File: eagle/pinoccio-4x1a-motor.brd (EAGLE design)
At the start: 25.4 x 43.2 mm, 27 parts, among them IC1 74LVC1G04DBV, IC2 74LVC1G04DBV, IC3 74LVC1G04DBV, IC4 74LVC1G04DBV, J1 POWER_JACKPTH, U1 TB6621FNG, U2 TB6621FNG

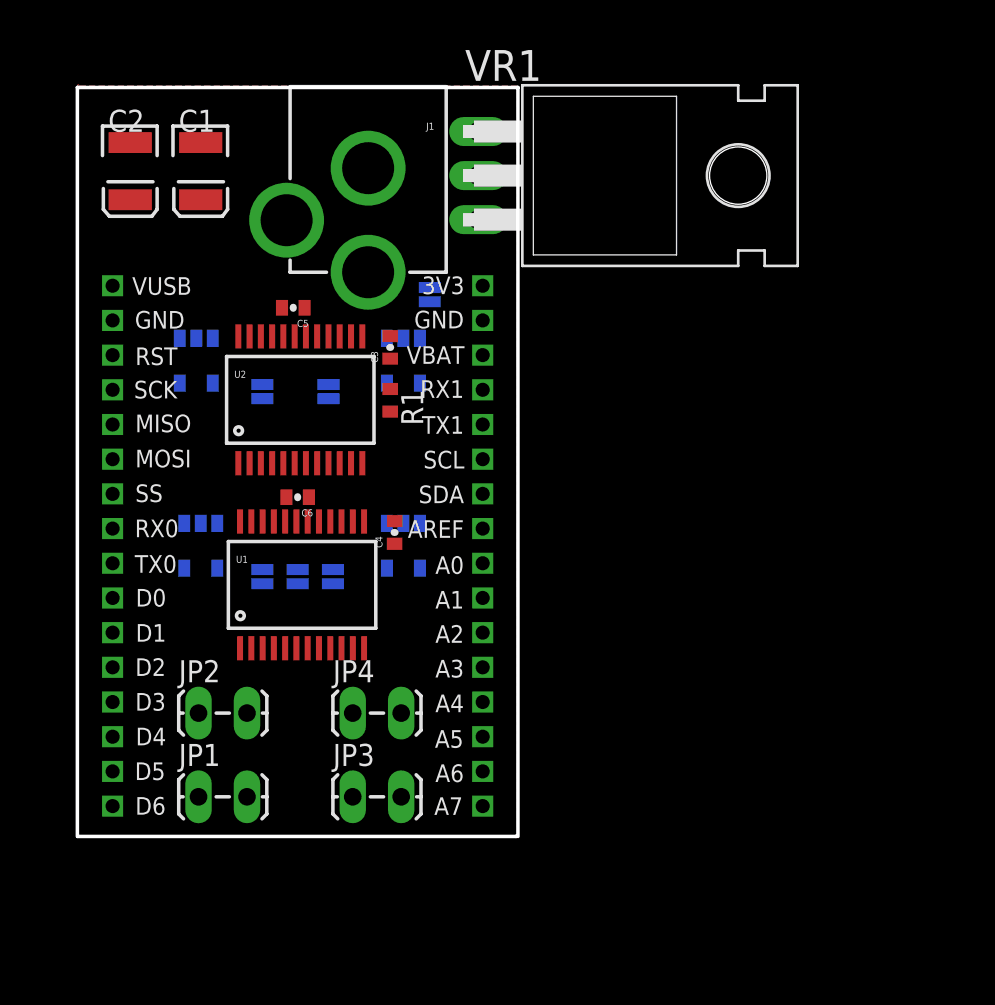
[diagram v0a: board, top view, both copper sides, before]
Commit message: Change layout onto an Arduino shield compatible board.
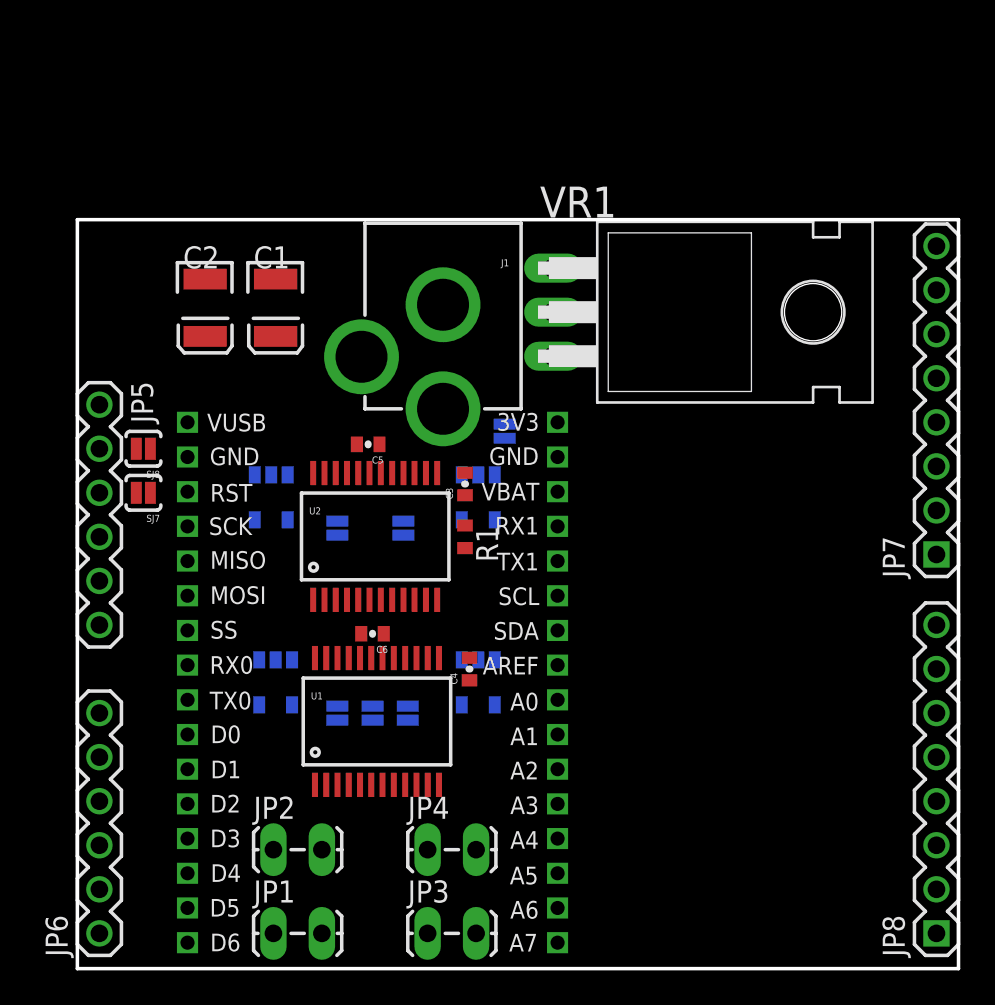
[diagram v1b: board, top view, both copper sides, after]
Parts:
- added JP5: Power, SparkFun:1X06
- added JP6: Analog, SparkFun:1X06
- added JP7: Digital2, SparkFun:1X08
- added JP8: Digital1, SparkFun:1X08
- added SJ7, SJ8: SOLDERJUMPERNC2, SparkFun-Passives:SJ_2S-NOTRACE
- moved C4 8.98 mm to (22.6, 17.3)
- moved C5 8.98 mm to (16.8, 30.2)
- moved C6 8.98 mm to (17.0, 19.3)
- moved J1 8.98 mm to (21.1, 46.0)
- moved JP3 8.98 mm to (20.3, 2.03)
- moved JP4 8.98 mm to (20.3, 6.86)
- moved SJ1 8.98 mm to (15.0, 14.7)
- moved SJ2 8.98 mm to (19.1, 14.7)
- moved SJ3 8.98 mm to (15.0, 25.4)
- moved SJ4 8.98 mm to (18.8, 25.4)
- moved SJ5 8.98 mm to (17.0, 14.7)
- moved SJ6 8.98 mm to (24.6, 31.0)
- moved U2 8.98 mm to (17.2, 24.9)
- moved C3 8.98 mm to (22.4, 27.9)
- moved IC2 8.98 mm to (23.1, 16.5)
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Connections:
- new net 3.3V: JP5.2, SJ8.2
- new net 5V: JP5.3, SJ7.2
- new net D10: JP7.3
- new net D11: JP7.4
- new net D12: JP7.5
- new net D13: JP7.6
- new net D7: JP8.8
- new net D8: JP7.1
- new net D9: JP7.2
- net A0: now also JP6.6
- net A1: now also JP6.5
- net A2: now also JP6.4
- net A3: now also JP6.3
- net A4: now also JP6.2
- net A5: now also JP6.1
- net AREF: now also JP7.8
- net D0: now also JP8.1
- net D1: now also JP8.2
- net D2: now also JP8.3
- net D3: now also JP8.4
- net D4: now also JP8.5
- net D5: now also JP8.6
- net D6: now also JP8.7
- net GND: now also JP5.4, JP5.5, JP7.7
- net RESET: now also JP5.1
- net VCC-AE: now also SJ7.1, SJ8.1
- net VUSB: now also JP5.6
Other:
- board size 25.4 x 43.2 mm -> 50.8 x 43.2 mm

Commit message: High current traces routed.
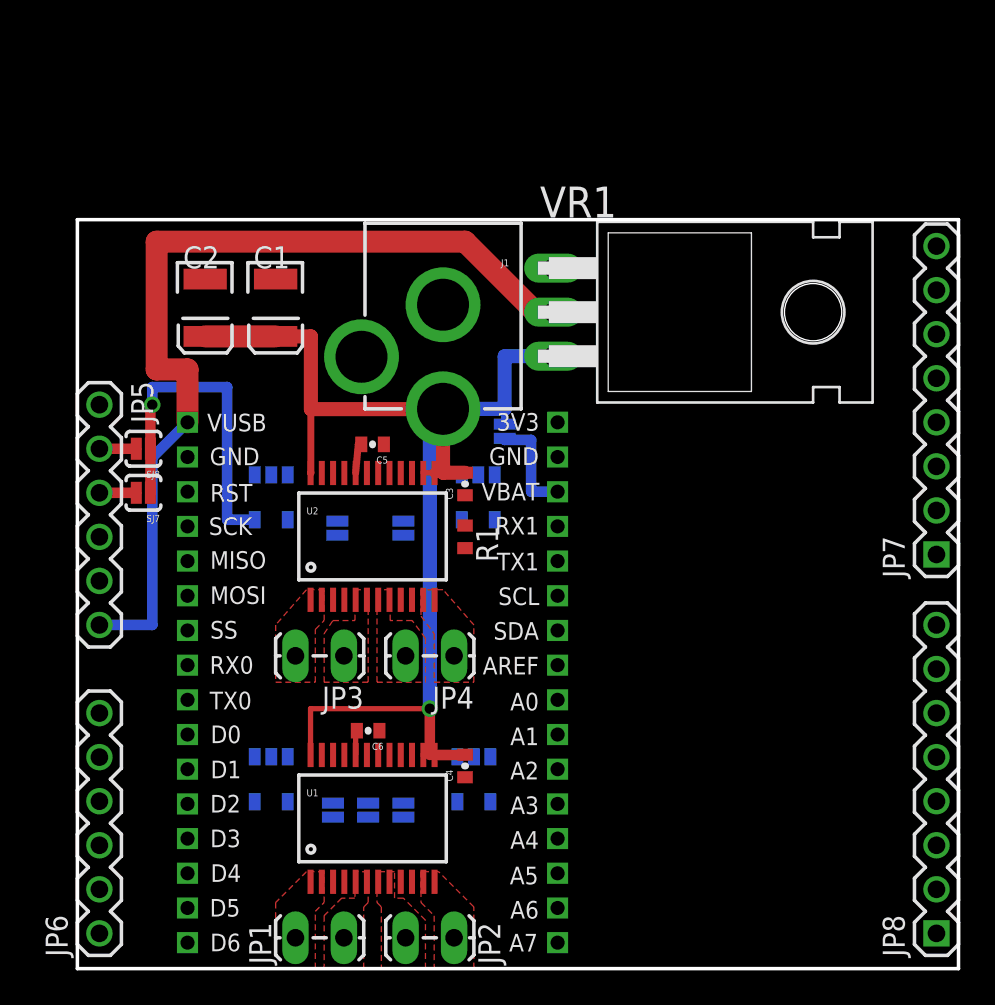
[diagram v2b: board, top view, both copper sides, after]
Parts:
- moved JP3 16.8 mm to (15.2, 18.0), turned to 180 degrees
- moved JP2 11.4 mm to (21.6, 1.78), turned to 180 degrees
- moved JP4 11.2 mm to (21.6, 18.0), turned to 180 degrees
- moved IC1 5.59 mm to (11.2, 10.9)
- moved IC2 5.59 mm to (22.9, 10.9)
- moved C4 5.59 mm to (22.4, 11.7)
- moved C6 5.59 mm to (16.8, 13.7)
- moved SJ1 5.59 mm to (14.7, 9.14)
- moved SJ2 5.59 mm to (18.8, 9.14)
- moved SJ5 5.59 mm to (16.8, 9.14)
- moved U1 5.59 mm to (17.0, 8.66)
- moved JP1 3.82 mm to (15.2, 1.78), turned to 180 degrees
- moved C5 0.25 mm to (17.0, 30.2)
- moved U2 0.15 mm to (17.0, 24.9)
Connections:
- net N$8 renamed M4-
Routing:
- net V+: track 0.00 -> 72.1 mm, vias 0 -> 1
- net VUSB: track 0.00 -> 52.3 mm
- net VCC-AE: track 0.00 -> 23.1 mm, vias 0 -> 1
- net VBAT-AE: track 0.00 -> 6.13 mm
- net 5V: track 0.00 -> 2.13 mm
- net 3.3V: track 0.00 -> 2.13 mm
- added copper zone on layer 1, net M1+
- added copper zone on layer 1, net M1-
- added copper zone on layer 1, net M2+
- added copper zone on layer 1, net M2-
- added copper zone on layer 1, net M3+
- added copper zone on layer 1, net M3-
- added copper zone on layer 1, net M4+
- added copper zone on layer 1, net M4-
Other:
- board text removed: "Pinoccio(tm) Proto v0.9"
